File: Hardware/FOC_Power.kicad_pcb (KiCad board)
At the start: 2 copper layers, 41 parts, among them J1 Conn_01x03_Male, J2 Conn_01x03_Male, Q1 IRF7480M, Q10 IRF7480M, Q11 IRF7480M, Q12 IRF7480M, Q2 IRF7480M, Q3 IRF7480M, Q4 IRF7480M, Q5 IRF7480M, Q6 IRF7480M, Q7 IRF7480M, Q8 IRF7480M, Q9 IRF7480M, U1 STM32F405RGTx, U2 DRV8323HRTAR, U3 DRV8323HRTAR

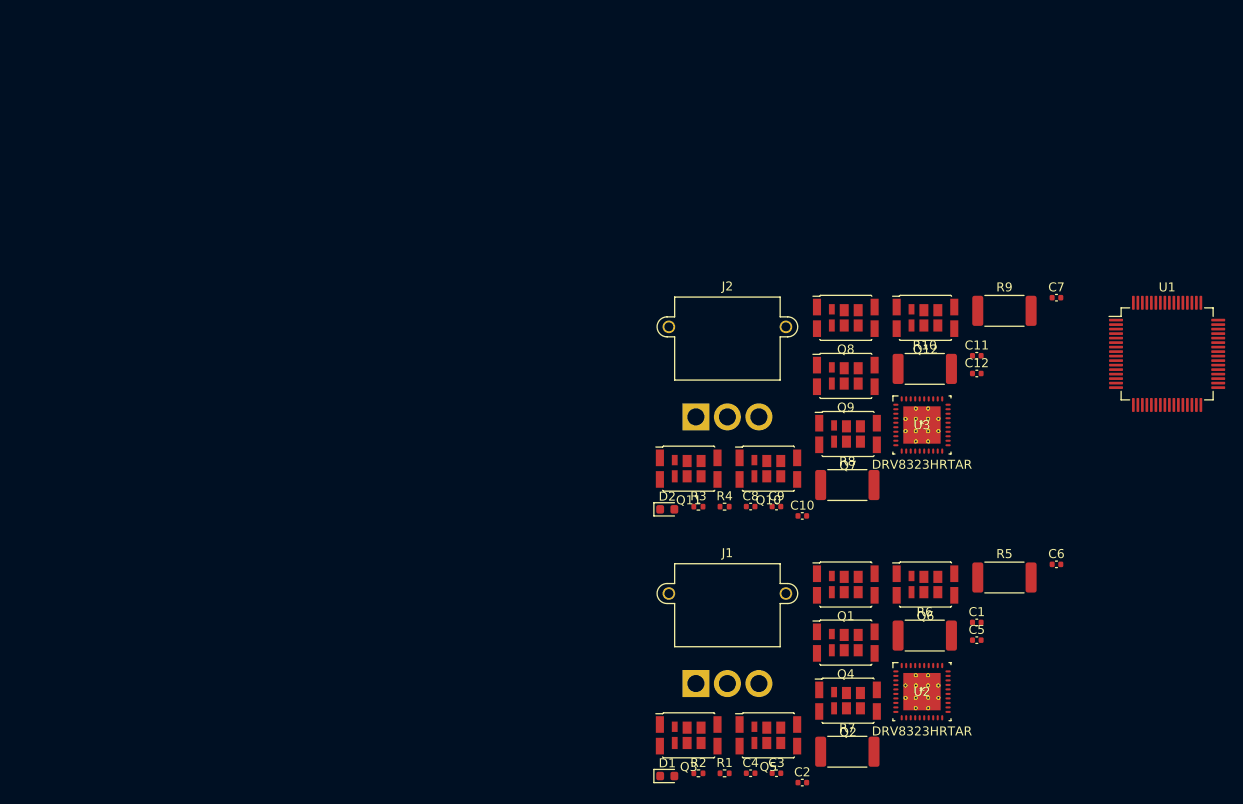
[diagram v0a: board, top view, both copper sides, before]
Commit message: Init FreeRTOS
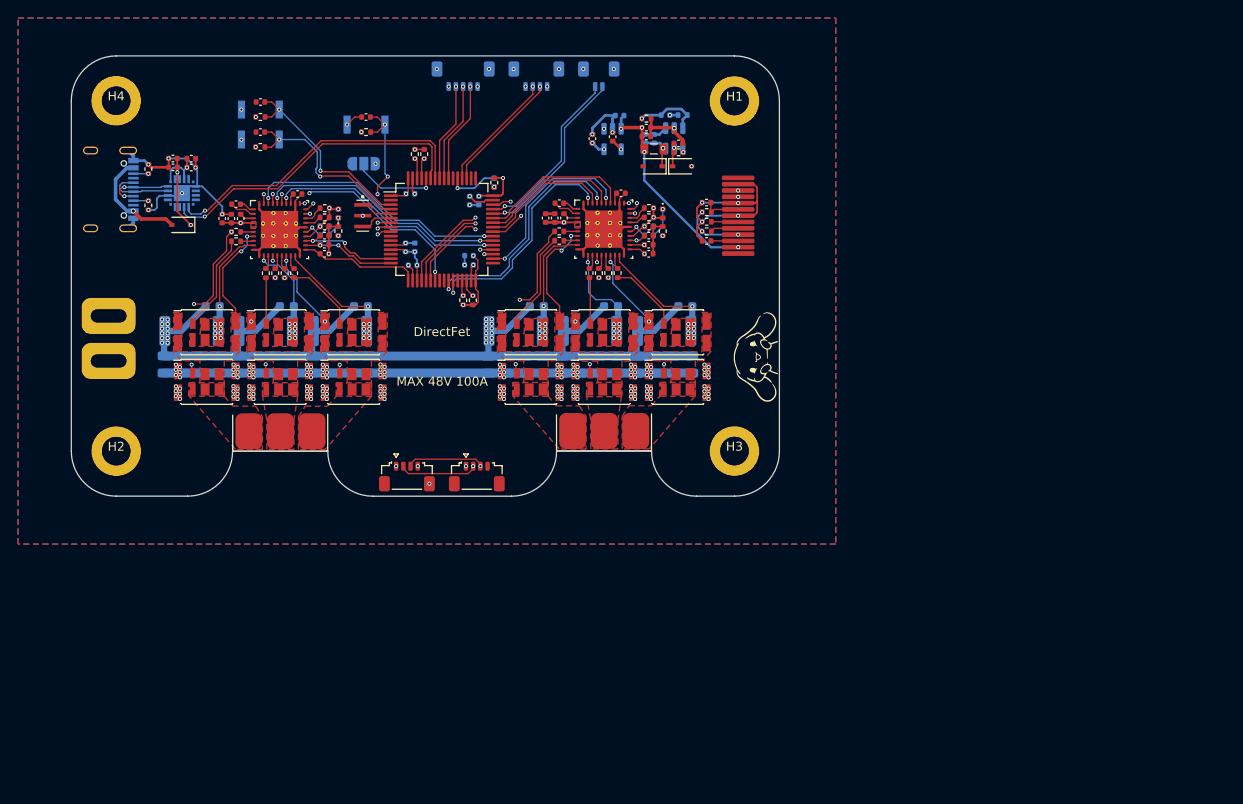
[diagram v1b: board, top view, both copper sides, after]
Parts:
- added C13: 0.1uF, Capacitor_SMD:C_0402_1005Metric, B.Cu at (72.7, 46.4)
- added C14: 0.1uF, Capacitor_SMD:C_0402_1005Metric, B.Cu at (66.7, 45.5)
- added C15: 0.1uF, Capacitor_SMD:C_0402_1005Metric, B.Cu at (65.6, 45.5)
- added C16: 2.2uF, Capacitor_SMD:C_0402_1005Metric, B.Cu at (72.7, 47.4)
- added C17: 2.2uF, Capacitor_SMD:C_0402_1005Metric, B.Cu at (72.8, 40.3)
- added C18: 10uF, Capacitor_SMD:C_0402_1005Metric, F.Cu at (95.9, 33.9)
- added C19: 4.7uF, Capacitor_SMD:C_0402_1005Metric, F.Cu at (39.8, 36.6)
- added C20: 0.1uF, Capacitor_SMD:C_0402_1005Metric, F.Cu at (39.8, 35.6)
- added C21: 4.7uF, Capacitor_SMD:C_0402_1005Metric, F.Cu at (41.8, 35.6)
- added C22: 0.1uF, Capacitor_SMD:C_0402_1005Metric, F.Cu at (41.8, 36.6)
- added C23: 0.1uF, Capacitor_SMD:C_0402_1005Metric, B.Cu at (92.3, 33.4)
- added C24: 0.1uF, Capacitor_SMD:C_0402_1005Metric, B.Cu at (93.3, 33.4)
- added C25: 0.1uF, Capacitor_SMD:C_0402_1005Metric, F.Cu at (92.4, 33.2)
- added C26: 100pF, Capacitor_SMD:C_0402_1005Metric, B.Cu at (94.5, 30.8)
- added C27: 10uF, Capacitor_SMD:C_0402_1005Metric, F.Cu at (92.4, 32.2)
- added C28: 0.1uF, Capacitor_SMD:C_0402_1005Metric, B.Cu at (89.4, 30.8)
- added C29: 10uF, Capacitor_SMD:C_0402_1005Metric, F.Cu at (99.1, 44.8)
- added C30: 10uF, Capacitor_SMD:C_0402_1005Metric, F.Cu at (99.1, 40.5)
- added C31: 0.1uF, Capacitor_SMD:C_0402_1005Metric, F.Cu at (86.4, 33.4)
- added C32: 10nF, Capacitor_SMD:C_0402_1005Metric, F.Cu at (88.6, 33.2)
- added C33: 10uF, Capacitor_SMD:C_0402_1005Metric, B.Cu at (86.4, 33.4)
- added C34: 2.2uF, Capacitor_SMD:C_0402_1005Metric, F.Cu at (92.7, 46.2)
- added C35: 2.2uF, Capacitor_SMD:C_0402_1005Metric, F.Cu at (92.7, 45.2)
- added C36: 2.2uF, Capacitor_SMD:C_0402_1005Metric, F.Cu at (92.7, 44.2)
- added C37: 1uF, Capacitor_SMD:C_0603_1608Metric, B.Cu at (96.7, 52.0)
- added C38: 1uF, Capacitor_SMD:C_0603_1608Metric, B.Cu at (88.5, 52.0)
- added C39: 1uF, Capacitor_SMD:C_0603_1608Metric, B.Cu at (80.2, 52.0)
- added C40: 220uF, Capacitor_SMD:C_0805_2012Metric, B.Cu at (93.3, 58.5)
- added C41: 220uF, Capacitor_SMD:C_0805_2012Metric, B.Cu at (91.3, 58.5)
- added C42: 220uF, Capacitor_SMD:C_0805_2012Metric, B.Cu at (97.4, 58.5)
- added C43: 220uF, Capacitor_SMD:C_0805_2012Metric, B.Cu at (95.4, 58.5)
- added C44: 4.7uF, Capacitor_SMD:C_0402_1005Metric, F.Cu at (45.3, 42.3)
- added C45: 1uF, Capacitor_SMD:C_0402_1005Metric, F.Cu at (53.7, 39.6)
- added C46: 0.1uF, Capacitor_SMD:C_0402_1005Metric, F.Cu at (56.6, 43.2)
- added C47: 0.1uF, Capacitor_SMD:C_0402_1005Metric, F.Cu at (46.3, 42.3)
- added C48: 1uF, Capacitor_SMD:C_0402_1005Metric, F.Cu at (47.3, 42.3)
- added C49: 47nF, Capacitor_SMD:C_0402_1005Metric, F.Cu at (46.8, 40.7)
- added C50: 2.2uF, Capacitor_SMD:C_0402_1005Metric, F.Cu at (56.6, 46.2)
- added C51: 2.2uF, Capacitor_SMD:C_0402_1005Metric, F.Cu at (56.6, 45.2)
- added C52: 2.2uF, Capacitor_SMD:C_0402_1005Metric, F.Cu at (56.6, 44.2)
- added C53: 1uF, Capacitor_SMD:C_0603_1608Metric, B.Cu at (60.7, 52.1)
- added C54: 1uF, Capacitor_SMD:C_0603_1608Metric, B.Cu at (52.5, 52.0)
- added C55: 1uF, Capacitor_SMD:C_0603_1608Metric, B.Cu at (44.2, 52.0)
- added C56: 220uF, Capacitor_SMD:C_0805_2012Metric, B.Cu at (38.8, 58.5)
- added C57: 220uF, Capacitor_SMD:C_0805_2012Metric, B.Cu at (42.9, 58.5)
- added C58: 220uF, Capacitor_SMD:C_0805_2012Metric, B.Cu at (61.4, 58.5)
- added C59: 220uF, Capacitor_SMD:C_0805_2012Metric, B.Cu at (44.9, 58.5)
- added C60: 220uF, Capacitor_SMD:C_0805_2012Metric, B.Cu at (78.9, 58.5)
- added C61: 220uF, Capacitor_SMD:C_0805_2012Metric, B.Cu at (80.9, 58.5)
- added C62: 220uF, Capacitor_SMD:C_0805_2012Metric, B.Cu at (76.9, 58.5)
- added C63: 220uF, Capacitor_SMD:C_0805_2012Metric, B.Cu at (83.1, 58.5)
- added C64: 220uF, Capacitor_SMD:C_0805_2012Metric, B.Cu at (87.1, 58.5)
- added C65: 220uF, Capacitor_SMD:C_0805_2012Metric, B.Cu at (89.2, 58.5)
- added C66: 220uF, Capacitor_SMD:C_0805_2012Metric, B.Cu at (74.8, 58.5)
- added C67: 220uF, Capacitor_SMD:C_0805_2012Metric, B.Cu at (85.1, 58.5)
- added C68: 220uF, Capacitor_SMD:C_0805_2012Metric, B.Cu at (47.0, 58.5)
- added C69: 220uF, Capacitor_SMD:C_0805_2012Metric, B.Cu at (57.3, 58.5)
- added C70: 220uF, Capacitor_SMD:C_0805_2012Metric, B.Cu at (40.9, 58.5)
- added C71: 220uF, Capacitor_SMD:C_0805_2012Metric, B.Cu at (55.3, 58.5)
- added C72: 220uF, Capacitor_SMD:C_0805_2012Metric, B.Cu at (51.1, 58.5)
- added C73: 220uF, Capacitor_SMD:C_0805_2012Metric, B.Cu at (49.1, 58.5)
- added C74: 220uF, Capacitor_SMD:C_0805_2012Metric, B.Cu at (53.1, 58.5)
- added C75: 220uF, Capacitor_SMD:C_0805_2012Metric, B.Cu at (59.3, 58.5)
- added D3: B5819WS, Diode_SMD:D_SOD-323, F.Cu at (96.4, 36.5)
- added D4: B5819WS, Diode_SMD:D_SOD-323, F.Cu at (93.1, 36.5)
- added D7: B5819WS, Diode_SMD:D_SOD-323, F.Cu at (40.7, 43.0)
- added D8: LED, LED_SMD:LED_0402_1005Metric, F.Cu at (58.2, 41.7)
- added ENC0: ENC0, Connector_JST:JST_SUR_SM04B-SURS-TF_1x04-1MP_P0.80mm_Horizontal, F.Cu at (73.6, 70.9)
- added ENC1: ENC1, Connector_JST:JST_SUR_SM04B-SURS-TF_1x04-1MP_P0.80mm_Horizontal, F.Cu at (65.8, 70.9)
- added G***: LOGO, Audio_Module:Cine, F.Cu at (104.9, 57.7)
- added G***: LOGO, Audio_Module:Cine, B.Cu at (104.8, 57.8)
- added H1: Hole, Userlib:Hole, F.Cu at (102.2, 29.2)
- added H2: Hole, Userlib:Hole, F.Cu at (33.5, 68.1)
- added H3: Hole, Userlib:Hole, F.Cu at (102.2, 68.1)
- added H4: Hole, Userlib:Hole, F.Cu at (33.5, 29.2)
- added J3: XT30, Connector_AMASS:XT30_SMD, F.Cu at (29.6, 55.6)
- added J7: Conn_01x05_Male, Connector_JST:JST_SUR_SM05B-SURS-TF_1x05-1MP_P0.80mm_Horizontal, B.Cu at (72.0, 26.5)
- added J8: Conn_01x02_Male, Connector_JST:JST_SUR_SM02B-SURS-TF_1x02-1MP_P0.80mm_Horizontal, B.Cu at (87.1, 26.5)
- added J9: Conn_01x04_Male, Connector_JST:JST_SUR_SM04B-SURS-TF_1x04-1MP_P0.80mm_Horizontal, B.Cu at (80.2, 26.5)
- added JP1: SolderJumper_3_Open, Jumper:SolderJumper-3_P1.3mm_Open_RoundedPad1.0x1.5mm, B.Cu at (61.0, 36.2)
- added L1: 6.8uH, Inductor_SMD:L_0805_2012Metric, F.Cu at (93.2, 34.6)
- added MOTOR1: Motor1, Connector_AMASS:MR30_SMD, F.Cu at (51.7, 69.6)
- added R11: 10K, Resistor_SMD:R_0402_1005Metric, F.Cu at (75.5, 38.3)
- added R12: 10K, Resistor_SMD:R_0402_1005Metric, F.Cu at (49.5, 31.0)
- added R13: 10K, Resistor_SMD:R_0402_1005Metric, F.Cu at (49.5, 34.3)
- added R14: 1M, Resistor_SMD:R_0402_1005Metric, F.Cu at (96.0, 34.9)
- added R15: 10K, Resistor_SMD:R_0402_1005Metric, B.Cu at (96.4, 30.8)
- added R16: 1.8K, Resistor_SMD:R_0402_1005Metric, F.Cu at (92.4, 31.2)
- added R17: 560K, Resistor_SMD:R_0402_1005Metric, F.Cu at (99.1, 42.6)
- added R18: 4.7K, Resistor_SMD:R_0402_1005Metric, F.Cu at (99.1, 43.7)
- added R19: 10K, Resistor_SMD:R_0402_1005Metric, F.Cu at (99.1, 41.6)
- added R20: 5K1, Resistor_SMD:R_0402_1005Metric, F.Cu at (37.1, 40.8)
- added R21: 5K1, Resistor_SMD:R_0402_1005Metric, F.Cu at (37.1, 36.8)
- added R22: 18K, Resistor_SMD:R_0402_1005Metric, F.Cu at (92.7, 42.2)
- added R23: 18K, Resistor_SMD:R_0402_1005Metric, F.Cu at (92.7, 41.1)
- added R24: 47K, Resistor_SMD:R_0402_1005Metric, F.Cu at (94.2, 43.7)
- added R25: 2.2R, Resistor_SMD:R_0402_1005Metric, F.Cu at (46.8, 43.8)
- added R26: 2.2R, Resistor_SMD:R_0402_1005Metric, F.Cu at (46.8, 44.8)
- added R27: 330R, Resistor_SMD:R_0402_1005Metric, B.Cu at (56.7, 44.2)
- added R28: 1K, Resistor_SMD:R_0402_1005Metric, B.Cu at (56.7, 43.1)
- added R29: 18K, Resistor_SMD:R_0402_1005Metric, F.Cu at (56.7, 42.2)
- added R30: 18K, Resistor_SMD:R_0402_1005Metric, F.Cu at (56.7, 41.1)
- added R31: 47K, Resistor_SMD:R_0402_1005Metric, F.Cu at (58.2, 43.7)
- added R32: 5mR, Resistor_SMD:R_2512_6332Metric, B.Cu at (41.9, 54.8)
- added R33: 5mR, Resistor_SMD:R_2512_6332Metric, B.Cu at (50.1, 54.8)
- added R34: 5mR, Resistor_SMD:R_2512_6332Metric, B.Cu at (58.4, 54.8)
- added R35: 2.2R, Resistor_SMD:R_0402_1005Metric, F.Cu at (51.2, 48.4)
- added R36: 2.2R, Resistor_SMD:R_0402_1005Metric, F.Cu at (50.1, 48.4)
- added R37: 2.2R, Resistor_SMD:R_0402_1005Metric, F.Cu at (52.2, 48.4)
- added R38: 2.2R, Resistor_SMD:R_0402_1005Metric, F.Cu at (53.3, 48.4)
- added R39: 2.2R, Resistor_SMD:R_0402_1005Metric, F.Cu at (82.7, 43.7)
- added R40: 2.2R, Resistor_SMD:R_0402_1005Metric, F.Cu at (82.7, 44.8)
- added R41: 2.2R, Resistor_SMD:R_0402_1005Metric, F.Cu at (87.1, 48.3)
- added R42: 2.2R, Resistor_SMD:R_0402_1005Metric, F.Cu at (86.1, 48.3)
- added R43: 2.2R, Resistor_SMD:R_0402_1005Metric, F.Cu at (88.2, 48.3)
- added R44: 2.2R, Resistor_SMD:R_0402_1005Metric, F.Cu at (89.2, 48.3)
- added S: ENT, Button_Switch_SMD:SKRK, B.Cu at (49.5, 30.2)
- added S1: RST, Button_Switch_SMD:SKRK, B.Cu at (61.3, 31.9)
- added S3: SEL, Button_Switch_SMD:SKRK, B.Cu at (49.5, 33.5)
- added U4: CP2102N-Axx-xQFN20, Package_DFN_QFN:SiliconLabs_QFN-20-1EP_3x3mm_P0.5mm_EP1.8x1.8mm, B.Cu at (40.8, 39.5)
- added U5: OLED-12880, Userlib:OLED-12880, F.Cu at (102.6, 42.0)
- added U6: LP2992-3V3, Package_TO_SOT_SMD:SOT-23-5, B.Cu at (88.6, 33.5)
- added U7: DRV8323HRTAR, Userlib:DRV8323HRTAR, F.Cu at (51.6, 43.5)
- added Y1: CSTCE12M0G15L08-R0, Crystal:OSC_CSTCE12M0G15L08-R0, F.Cu at (60.9, 42.0)
- C10, R1, R2, R5, R6, R7: moved to B.Cu
- C11: value 1uF -> 0.1uF; moved to B.Cu
- C12: value 47nF -> 0.1uF; moved to B.Cu
- C7: value 4.7uF -> 0.1uF
- C8: value 1uF -> 0.1uF
- D1: footprint LED_SMD:LED_0603_1608Metric -> LED_SMD:LED_0402_1005Metric
- D2: footprint LED_SMD:LED_0603_1608Metric -> LED_SMD:LED_0402_1005Metric; moved to B.Cu
- J1: value Conn_01x03_Male -> Motor0; footprint Connector_AMASS:AMASS_MR30PW-M_1x03_P3.50mm_Horizontal -> Connector_AMASS:MR30_SMD
- J2: value Conn_01x03_Male -> USB_C_Receptacle_USB2.0; footprint Connector_AMASS:AMASS_MR30PW-M_1x03_P3.50mm_Horizontal -> Connector_USB:USB_C_Receptacle_Palconn_UTC16-G; moved to B.Cu
- R10, R8, R9: value 5mR -> 4.7K; footprint Resistor_SMD:R_2512_6332Metric -> Resistor_SMD:R_0402_1005Metric
- R3: value 330R -> 10K
- R4: value 1K -> 4.7K
- U3: value DRV8323HRTAR -> ME3116; footprint Userlib:DRV8323HRTAR -> Package_TO_SOT_SMD:SOT-23-6; moved to B.Cu
- moved U1 81.7 mm to (69.7, 43.5)
- moved C7 79.3 mm to (61.3, 31.0), turned to 180 degrees
- moved Q7 71.5 mm to (43.6, 60.4)
- moved Q8 71.0 mm to (43.6, 54.9)
- moved C9 70.8 mm to (49.5, 32.7), turned to 180 degrees
- moved C8 70.6 mm to (49.5, 29.3), turned to 180 degrees
- moved J2 69.7 mm to (32.9, 39.1), turned to 90 degrees
- moved C2 68.5 mm to (89.6, 39.5)
- moved C6 68.2 mm to (82.7, 40.6)
- moved R9 67.8 mm to (66.7, 35.1), turned to 90 degrees
- moved C1 65.7 mm to (81.2, 42.2), turned to 90 degrees
- moved C5 65.6 mm to (83.2, 42.2), turned to 90 degrees
- moved C11 65.4 mm to (66.2, 39.5), turned to 180 degrees
- moved C4 65.4 mm to (82.2, 42.2), turned to 90 degrees
- moved C12 63.8 mm to (66.4, 47.5)
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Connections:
- net /Motor1/FAULT1 renamed /FAULT0
- C10 pad 1: +12V -> GND
- C10 pad 2: GND -> +3V3
- C11 pad 1: +12V -> GND
- C11 pad 2: Net-(C11-Pad2) -> +3V3
- C12 pad 1: Net-(C12-Pad1) -> GND
- C12 pad 2: Net-(C12-Pad2) -> +3V3
- C7 pad 1: +12V -> /NRST
- C8 pad 1: Net-(C8-Pad1) -> /KEY_ENT
- C9 pad 1: +3V3 -> /KEY_SEL
- D2 pad 1: Net-(D2-Pad1) -> /User_LED
- D2 pad 2: +3V3 -> Net-(D2-Pad2)
- J1 pad 1: /Motor1/SHC -> /Motor0/SHC
- J1 pad 2: /Motor1/SHB -> /Motor0/SHB
- J1 pad 3: /Motor1/SHA -> /Motor0/SHA
- Q1 pad 2: /Motor1/GHA -> Net-(Q1-Pad2)
- Q1 pad 3: /Motor1/SHA -> /Motor0/SHA
- Q10 pad 1: /Motor2/SHB -> /Motor1/SHB
- Q10 pad 2: /Motor2/GLB -> Net-(Q10-Pad2)
- Q10 pad 3: /Motor2/SPB -> /Motor1/SPB
- Q11 pad 2: /Motor2/GHC -> Net-(Q11-Pad2)
- Q11 pad 3: /Motor2/SHC -> /Motor1/SHC
- Q12 pad 1: /Motor2/SHC -> /Motor1/SHC
- Q12 pad 2: /Motor2/GLC -> Net-(Q12-Pad2)
- Q12 pad 3: /Motor2/SPC -> /Motor1/SPC
- Q2 pad 1: /Motor1/SHA -> /Motor0/SHA
- Q2 pad 2: /Motor1/GLA -> Net-(Q2-Pad2)
- Q2 pad 3: /Motor1/SPA -> /Motor0/SPA
- Q3 pad 2: /Motor1/GHB -> Net-(Q3-Pad2)
- Q3 pad 3: /Motor1/SHB -> /Motor0/SHB
- Q4 pad 1: /Motor1/SHB -> /Motor0/SHB
- Q4 pad 2: /Motor1/GLB -> Net-(Q4-Pad2)
- Q4 pad 3: /Motor1/SPB -> /Motor0/SPB
- Q5 pad 2: /Motor1/GHC -> Net-(Q5-Pad2)
- Q5 pad 3: /Motor1/SHC -> /Motor0/SHC
- Q6 pad 1: /Motor1/SHC -> /Motor0/SHC
- Q6 pad 2: /Motor1/GLC -> Net-(Q6-Pad2)
- Q6 pad 3: /Motor1/SPC -> /Motor0/SPC
- Q7 pad 2: /Motor2/GHA -> Net-(Q7-Pad2)
- Q7 pad 3: /Motor2/SHA -> /Motor1/SHA
- Q8 pad 1: /Motor2/SHA -> /Motor1/SHA
- Q8 pad 2: /Motor2/GLA -> Net-(Q8-Pad2)
- Q8 pad 3: /Motor2/SPA -> /Motor1/SPA
- Q9 pad 2: /Motor2/GHB -> Net-(Q9-Pad2)
- Q9 pad 3: /Motor2/SHB -> /Motor1/SHB
- R10 pad 1: /Motor2/SPC -> /I2C1_SCL
- R10 pad 2: GND -> +3V3
- R3 pad 1: Net-(D2-Pad1) -> +3V3
- R3 pad 2: /Motor2/FAULT1 -> /NRST
- R4 pad 1: +3V3 -> /I2C2_SDA
- R4 pad 2: /Motor2/FAULT1 -> +3V3
- R5 pad 1: /Motor1/SPA -> /Motor0/SPA
- R6 pad 1: /Motor1/SPB -> /Motor0/SPB
- R7 pad 1: /Motor1/SPC -> /Motor0/SPC
- R8 pad 1: /Motor2/SPA -> /I2C2_SCL
- R8 pad 2: GND -> +3V3
- R9 pad 1: /Motor2/SPB -> /I2C1_SDA
- R9 pad 2: GND -> +3V3
- U1 pad 1: unconnected-(U1-Pad1) -> +3V3
- U1 pad 12: unconnected-(U1-Pad12) -> GND
- U1 pad 13: unconnected-(U1-Pad13) -> +3V3
- U1 pad 15: unconnected-(U1-Pad15) -> /SOA1
- U1 pad 16: unconnected-(U1-Pad16) -> /SOB1
- U1 pad 17: unconnected-(U1-Pad17) -> /SOC1
- U1 pad 18: unconnected-(U1-Pad18) -> GND
- U1 pad 19: unconnected-(U1-Pad19) -> +3V3
- U1 pad 20: unconnected-(U1-Pad20) -> /SOA0
- U1 pad 21: unconnected-(U1-Pad21) -> /SOB0
- U1 pad 22: unconnected-(U1-Pad22) -> /SOC0
- U1 pad 23: unconnected-(U1-Pad23) -> /INLA1
- U1 pad 26: unconnected-(U1-Pad26) -> /INLB0
- U1 pad 27: unconnected-(U1-Pad27) -> /INLC0
- U1 pad 29: unconnected-(U1-Pad29) -> /I2C2_SCL
- U1 pad 3: unconnected-(U1-Pad3) -> /KEY_ENT
- U1 pad 30: unconnected-(U1-Pad30) -> /I2C2_SDA
- U1 pad 31: unconnected-(U1-Pad31) -> /VCAP_1
- U1 pad 32: unconnected-(U1-Pad32) -> +3V3
- U1 pad 34: unconnected-(U1-Pad34) -> /INLA0
- U1 pad 35: unconnected-(U1-Pad35) -> /INLB1
- U1 pad 36: unconnected-(U1-Pad36) -> /INLC1
- U1 pad 37: unconnected-(U1-Pad37) -> /INHA1
- U1 pad 38: unconnected-(U1-Pad38) -> /INHB1
- U1 pad 39: unconnected-(U1-Pad39) -> /INHC1
- U1 pad 4: unconnected-(U1-Pad4) -> /KEY_SEL
- U1 pad 40: unconnected-(U1-Pad40) -> /EN0
- U1 pad 41: unconnected-(U1-Pad41) -> /INHC0
- U1 pad 42: unconnected-(U1-Pad42) -> /INHB0
- U1 pad 43: unconnected-(U1-Pad43) -> /INHA0
- U1 pad 44: unconnected-(U1-Pad44) -> /CAN1_RX
- U1 pad 45: unconnected-(U1-Pad45) -> /CAN1_TX
- U1 pad 46: unconnected-(U1-Pad46) -> /CAL0
- U1 pad 47: unconnected-(U1-Pad47) -> /VCAP_2
- U1 pad 48: unconnected-(U1-Pad48) -> +3V3
- U1 pad 5: unconnected-(U1-Pad5) -> /PH0
- U1 pad 51: unconnected-(U1-Pad51) -> /USART3_TX
- U1 pad 52: unconnected-(U1-Pad52) -> /USART3_RX
- U1 pad 53: unconnected-(U1-Pad53) -> /User_LED
- U1 pad 55: unconnected-(U1-Pad55) -> /SPI1_SCK
- U1 pad 56: unconnected-(U1-Pad56) -> /SPI1_MISO
- U1 pad 57: unconnected-(U1-Pad57) -> /SPI1_MOSI
- U1 pad 58: unconnected-(U1-Pad58) -> /USART1_TX
- U1 pad 59: unconnected-(U1-Pad59) -> /USART1_RX
- U1 pad 6: unconnected-(U1-Pad6) -> /PH1
- U1 pad 60: unconnected-(U1-Pad60) -> /BOOT0
- U1 pad 61: unconnected-(U1-Pad61) -> /I2C1_SCL
- U1 pad 62: unconnected-(U1-Pad62) -> /I2C1_SDA
- U1 pad 63: unconnected-(U1-Pad63) -> GND
- U1 pad 64: unconnected-(U1-Pad64) -> +3V3
- U1 pad 7: unconnected-(U1-Pad7) -> /NRST
- U1 pad 8: unconnected-(U1-Pad8) -> /EN1
- U1 pad 9: unconnected-(U1-Pad9) -> /CAL1
- U2 pad 12: /Motor1/SPB -> /Motor0/SPB
- U2 pad 13: /Motor1/GLB -> /Motor0/GLB
- U2 pad 14: /Motor1/SHB -> /Motor0/SHB
- U2 pad 15: /Motor1/GHB -> /Motor0/GHB
- U2 pad 16: /Motor1/GHC -> /Motor0/GHC
- U2 pad 17: /Motor1/SHC -> /Motor0/SHC
- U2 pad 18: /Motor1/GLC -> /Motor0/GLC
- U2 pad 19: /Motor1/SPC -> /Motor0/SPC
- U2 pad 21: /Motor1/SOC1 -> /SOC0
- U2 pad 22: /Motor1/SOB1 -> /SOB0
- U2 pad 23: /Motor1/SOA1 -> /SOA0
- U2 pad 26: unconnected-(U2-Pad26) -> GND
- U2 pad 27: unconnected-(U2-Pad27) -> Net-(R22-Pad2)
- U2 pad 28: unconnected-(U2-Pad28) -> Net-(R23-Pad2)
- U2 pad 29: unconnected-(U2-Pad29) -> Net-(R24-Pad2)
- U2 pad 30: /Motor1/EN1 -> /EN0
- U2 pad 31: /Motor1/CAL1 -> /CAL0
- U2 pad 34: /Motor1/INHA1 -> /INHA0
- U2 pad 35: /Motor1/INLA1 -> /INLA0
- U2 pad 36: /Motor1/INHB1 -> /INHB0
- U2 pad 37: /Motor1/INLB1 -> /INLB0
- U2 pad 38: /Motor1/INHC1 -> /INHC0
- U2 pad 39: /Motor1/INLC1 -> /INLC0
- U2 pad 5: unconnected-(U2-Pad5) -> +12V
- U2 pad 6: /Motor1/GHA -> /Motor0/GHA
- U2 pad 7: /Motor1/SHA -> /Motor0/SHA
- U2 pad 8: /Motor1/GLA -> /Motor0/GLA
- U2 pad 9: /Motor1/SPA -> /Motor0/SPA
- U2 pad V: (no net) -> GND
- U3 pad 1: Net-(C12-Pad2) -> Net-(C23-Pad2)
- U3 pad 2: Net-(C12-Pad1) -> GND
- U3 pad 3: Net-(C11-Pad2) -> Net-(C26-Pad2)
- U3 pad 4: +12V -> Net-(R14-Pad2)
- U3 pad 5: unconnected-(U3-Pad5) -> Net-(C18-Pad1)
- U3 pad 6: /Motor2/GHA -> Net-(C23-Pad1)
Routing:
- net GND: track 0.00 -> 221.2 mm, vias 0 -> 57
- net +3V3: track 0.00 -> 194.2 mm, vias 0 -> 29
- net +12V: track 0.00 -> 174.6 mm, vias 0 -> 147
- net +5V: track 0.00 -> 100.9 mm, vias 0 -> 8
- net /I2C1_SCL: track 0.00 -> 40.5 mm, vias 0 -> 2
- net /I2C1_SDA: track 0.00 -> 39.7 mm, vias 0 -> 2
- net /USART1_RX: track 0.00 -> 35.5 mm, vias 0 -> 1
- net /USART1_TX: track 0.00 -> 35.2 mm, vias 0 -> 1
- net /SOA0: track 0.00 -> 32.4 mm, vias 0 -> 2
- net /SOB0: track 0.00 -> 31.5 mm, vias 0 -> 2
- net /SOC0: track 0.00 -> 31.2 mm, vias 0 -> 2
- net /INLC1: track 0.00 -> 30.3 mm, vias 0 -> 2
- net /I2C2_SDA: track 0.00 -> 30.2 mm, vias 0 -> 2
- net /I2C2_SCL: track 0.00 -> 29.9 mm, vias 0 -> 2
- net /INHC1: track 0.00 -> 29.4 mm, vias 0 -> 2
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- added copper zone on F.Cu, net +12V
- added copper zone on In2.Cu, net +12V
- added copper zone on F.Cu, net /Motor0/SHA
- added copper zone on F.Cu, net /Motor0/SHB
- added copper zone on F.Cu, net /Motor0/SHC
- added copper zone on F.Cu, net /Motor0/SPA
- added copper zone on F.Cu, net /Motor0/SPB
- added copper zone on F.Cu, net /Motor0/SPC
- added copper zone on F.Cu, net /Motor1/SHA
- added copper zone on F.Cu, net /Motor1/SHB
- added copper zone on F.Cu, net /Motor1/SHC
- added copper zone on F.Cu, net /Motor1/SPA
- added copper zone on F.Cu, net /Motor1/SPB
- added copper zone on F.Cu, net /Motor1/SPC
- added copper zone on B.Cu, net GND
- added copper zone on F.Cu, net GND
- added copper zone on In1.Cu, net GND
- added copper zone on In2.Cu, net GND
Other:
- board outline added: 78.7 x 48.9 mm
- copper layers 2 -> 4
- board text added: "& Platformio"
- board text added: "+"
- board text added: "-"
- board text added: "0"
- board text added: "0 mm"
- board text added: "0.01 mm"
- board text added: "0.02"
- board text added: "0.035 mm"
- board text added: "1"
- board text added: "1.51 mm"
- board text added: "2023.1.5"
- board text added: "3.3"
- board text added: "4.5"
- board text added: "B.Cu"
- board text added: "B.Mask"
- board text added: "B.Paste"
- board text added: "B.Silkscreen"
- board text added: "BOOT0"
- board text added: "Bottom Silk Screen"
- board text added: "Bottom Solder Mask"
- board text added: "Bottom Solder Paste"
- board text added: "CAN"
- board text added: "Designed By MengBowen"
- board text added: "DirectFet"
- board text added: "ENC0"
- board text added: "ENC1"
- board text added: "Epsilon R（相对介电常数）"
- board text added: "F.Cu"
- board text added: "F.Mask"
- board text added: "F.Paste"
- board text added: "F.Silkscreen"
- board text added: "FOC_CTRL-V8.3"
- board text added: "FR4"
- board text added: "In1.Cu"
- board text added: "In2.Cu"
- board text added: "Loss Tangent（损耗角正切）"
- board text added: "MAX 48V 100A"
- board text added: "Motor0"
- board text added: "Motor1"
- board text added: "Not specified"
- board text added: "OLED"
- board text added: "Powered By Freertos & SimpleFOC"
- board text added: "SPI"
- board text added: "Top Silk Screen"
- board text added: "Top Solder Mask"
- board text added: "Top Solder Paste"
- board text added: "UART"
- board text added: "USB"
- board text added: "copper"
- board text added: "core"
- board text added: "prepreg"
- board text added: "层名称"
- board text added: "材料"
- board text added: "电介质层 1"
- board text added: "电介质层 2"
- board text added: "电介质层 3"
- board text added: "类型"
- board text added: "粗细 (mm)"
- board text added: "颜色"
